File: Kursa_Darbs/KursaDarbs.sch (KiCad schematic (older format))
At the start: 41 parts, among them J1 INPUT, J2 OUTPUT, Q1 MPSA42, Q2 MPSA42, Q3 BC546, Q4 MPSA42, Q5 BC546, Q6 Q_NPN_BCE, Q7 Q_PNP_BCE, Q8 IRF540N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

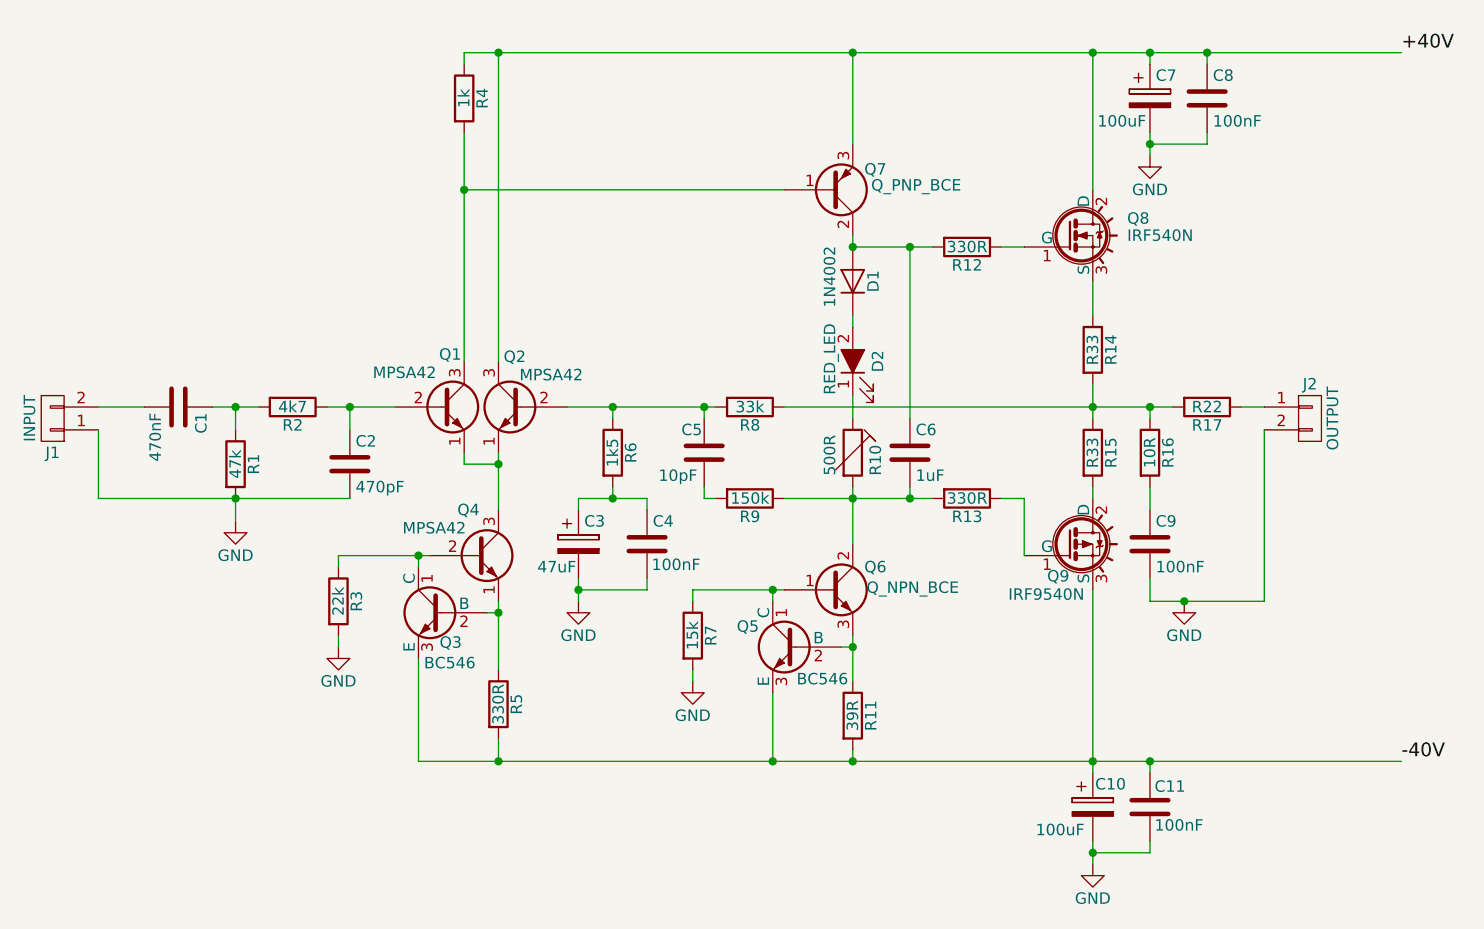
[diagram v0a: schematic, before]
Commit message: Kursa darba papildinajums, lekciju darbu nobeigums
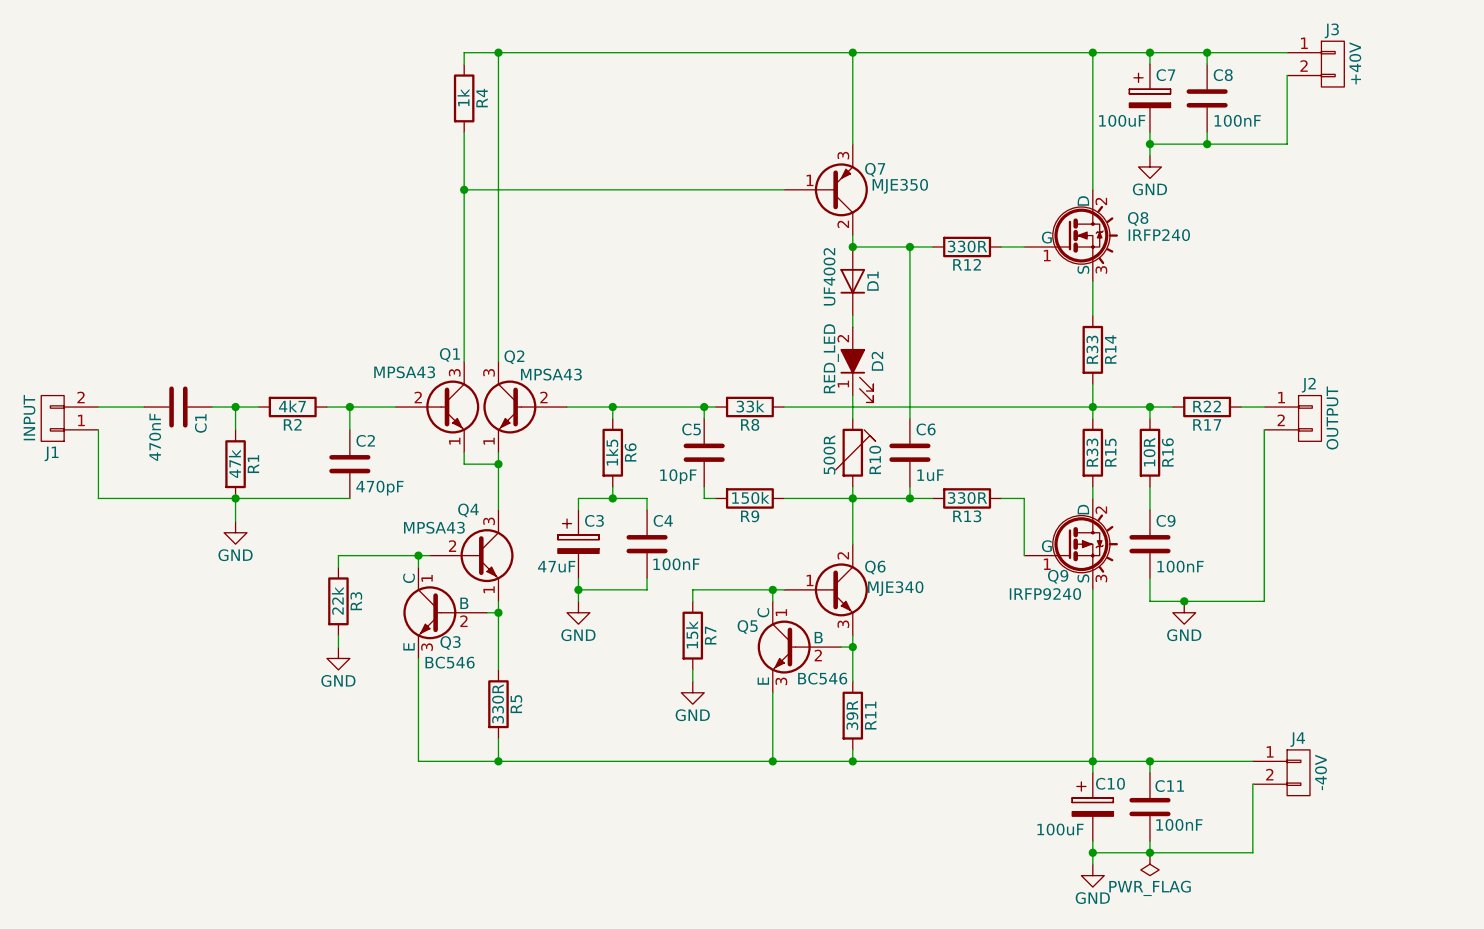
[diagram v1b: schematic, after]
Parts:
- added J3: +40V, symbol CONN_01X02
- added J4: -40V, symbol CONN_01X02
- C1: footprint (none) -> Capacitors_THT:C_Rect_L7.2mm_W4.5mm_P5.00mm_FKS2_FKP2_MKS2_MKP2
- C10, C3, C7: footprint (none) -> Capacitors_THT:CP_Radial_D8.0mm_P3.50mm
- C11, C4, C8, C9: footprint (none) -> Capacitors_THT:C_Rect_L7.2mm_W2.5mm_P5.00mm_FKS2_FKP2_MKS2_MKP2
- C2: footprint (none) -> Capacitors_THT:C_Disc_D5.0mm_W2.5mm_P5.00mm
- C5: footprint (none) -> Capacitors_THT:C_Disc_D6.0mm_W2.5mm_P5.00mm
- C6: footprint (none) -> Capacitors_THT:C_Rect_L7.2mm_W7.2mm_P5.00mm_FKS2_FKP2_MKS2_MKP2
- D1: value 1N4002 -> UF4002; footprint (none) -> Diodes_THT:D_DO-41_SOD81_P10.16mm_Horizontal
- D2: footprint (none) -> LEDs:LED_D5.0mm
- Q1, Q2, Q4: value MPSA42 -> MPSA43
- Q6: value Q_NPN_BCE -> MJE340; footprint (none) -> TO_SOT_Packages_THT:TO-126_Vertical
- Q7: value Q_PNP_BCE -> MJE350; footprint (none) -> TO_SOT_Packages_THT:TO-126_Vertical
- Q8: value IRF540N -> IRFP240
- Q9: value IRF9540N -> IRFP9240
- R10: footprint (none) -> Potentiometers:Potentiometer_Trimmer_Vishay_T73XW_Vertical
- R11: footprint (none) -> Resistors_THT:R_Axial_DIN0207_L6.3mm_D2.5mm_P10.16mm_Horizontal
- R14, R15, R16: footprint (none) -> Resistors_THT:R_Axial_DIN0617_L17.0mm_D6.0mm_P20.32mm_Horizontal
- R17: footprint (none) -> Resistors_THT:R_Axial_DIN0918_L18.0mm_D9.0mm_P22.86mm_Horizontal
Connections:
- net GND: now also J3.2 (P2), J4.2 (P2)
- net +40V: no longer names the net of C7.1, C8.1, Q2.3 (C), Q7.3 (E), Q8.2 (D), R4.1
- net +40V: now also J3.1 (P1)
- net -40V: no longer names the net of C10.1, C11.1, Q3.3 (E), Q5.3 (E), Q9.3 (S), R11.2, R5.2
- net -40V: now also J4.1 (P1)

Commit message: PCB Edit #1
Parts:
- J1, J2, J3, J4: footprint (none) -> Connectors:AK300-2
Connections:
- net GND: now also C10.1; no longer C10.2
- net at C11.1, J4.1 (P1), Q3.3 (E)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: now also C10.2; no longer C10.1
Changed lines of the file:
@@
 F 3 "http://www.mouser.com/ds/2/315/ABA0000C1047-947484.pdf" H 5650 4500 50  0001 C CNN
 	1    5650 4500
-	1    0    0    -1
+	-1   0    0    1
 $EndComp
 $Comp
@@
 F 0 "J2" H 6600 2950 50  0000 C CNN
 F 1 "OUTPUT" V 6700 2800 50  0000 C CNN
-F 2 "" H 6600 2800 50  0001 C CNN
+F 2 "Connectors:AK300-2" H 6600 2800 50  0001 C CNN
 F 3 "" H 6600 2800 50  0001 C CNN
 	1    6600 2800
@@
 F 0 "J1" H 1100 2950 50  0000 C CNN
 F 1 "INPUT" V 1200 2800 50  0000 C CNN
-F 2 "" H 1100 2800 50  0001 C CNN
+F 2 "Connectors:AK300-2" H 1100 2800 50  0001 C CNN
 F 3 "" H 1100 2800 50  0001 C CNN
 	1    1100 2800
@@
 F 0 "J3" H 6700 1400 50  0000 C CNN
 F 1 "+40V" V 6800 1250 50  0000 C CNN
-F 2 "" H 6700 1250 50  0001 C CNN
+F 2 "Connectors:AK300-2" H 6700 1250 50  0001 C CNN
 F 3 "" H 6700 1250 50  0001 C CNN
 	1    6700 1250
@@
 F 0 "J4" H 6550 4500 50  0000 C CNN
 F 1 "-40V" V 6650 4350 50  0000 C CNN
-F 2 "" H 6550 4350 50  0001 C CNN
+F 2 "Connectors:AK300-2" H 6550 4350 50  0001 C CNN
 F 3 "" H 6550 4350 50  0001 C CNN
 	1    6550 4350
